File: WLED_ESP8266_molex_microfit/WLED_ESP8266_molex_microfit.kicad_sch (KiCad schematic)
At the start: 62 parts, among them J1 Molex Micro-fit 2x1, J2 Molex Micro-fit 3x1, J3 Molex Micro-fit 2x1, J4 Molex Micro-fit 2x1, J6 Molex Micro-fit 2x1, J7 Molex Micro-fit 3x1, J8 Molex Micro-fit 3x1, Q1 AO3401A, Q2 AO3401A, U1 ESP-12F, U2 TPS54331DDAR, U3 TXS0102DCT, U4 TXS0102DCT, U6 ME6211A33M3G-N

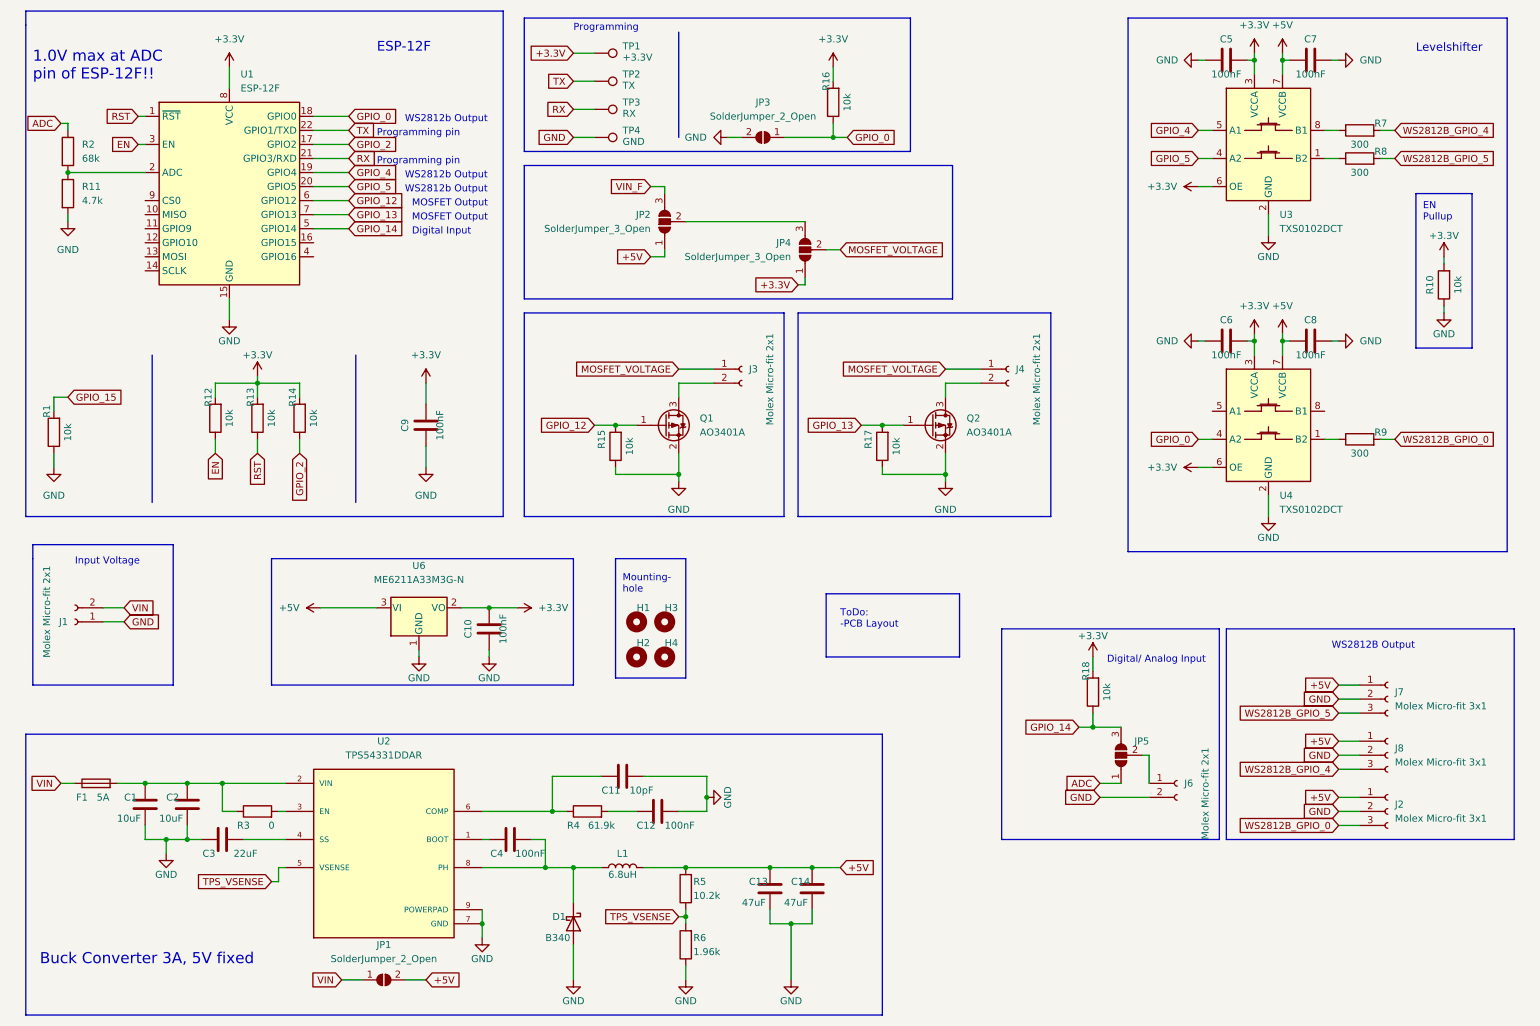
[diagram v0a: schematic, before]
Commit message: USB added
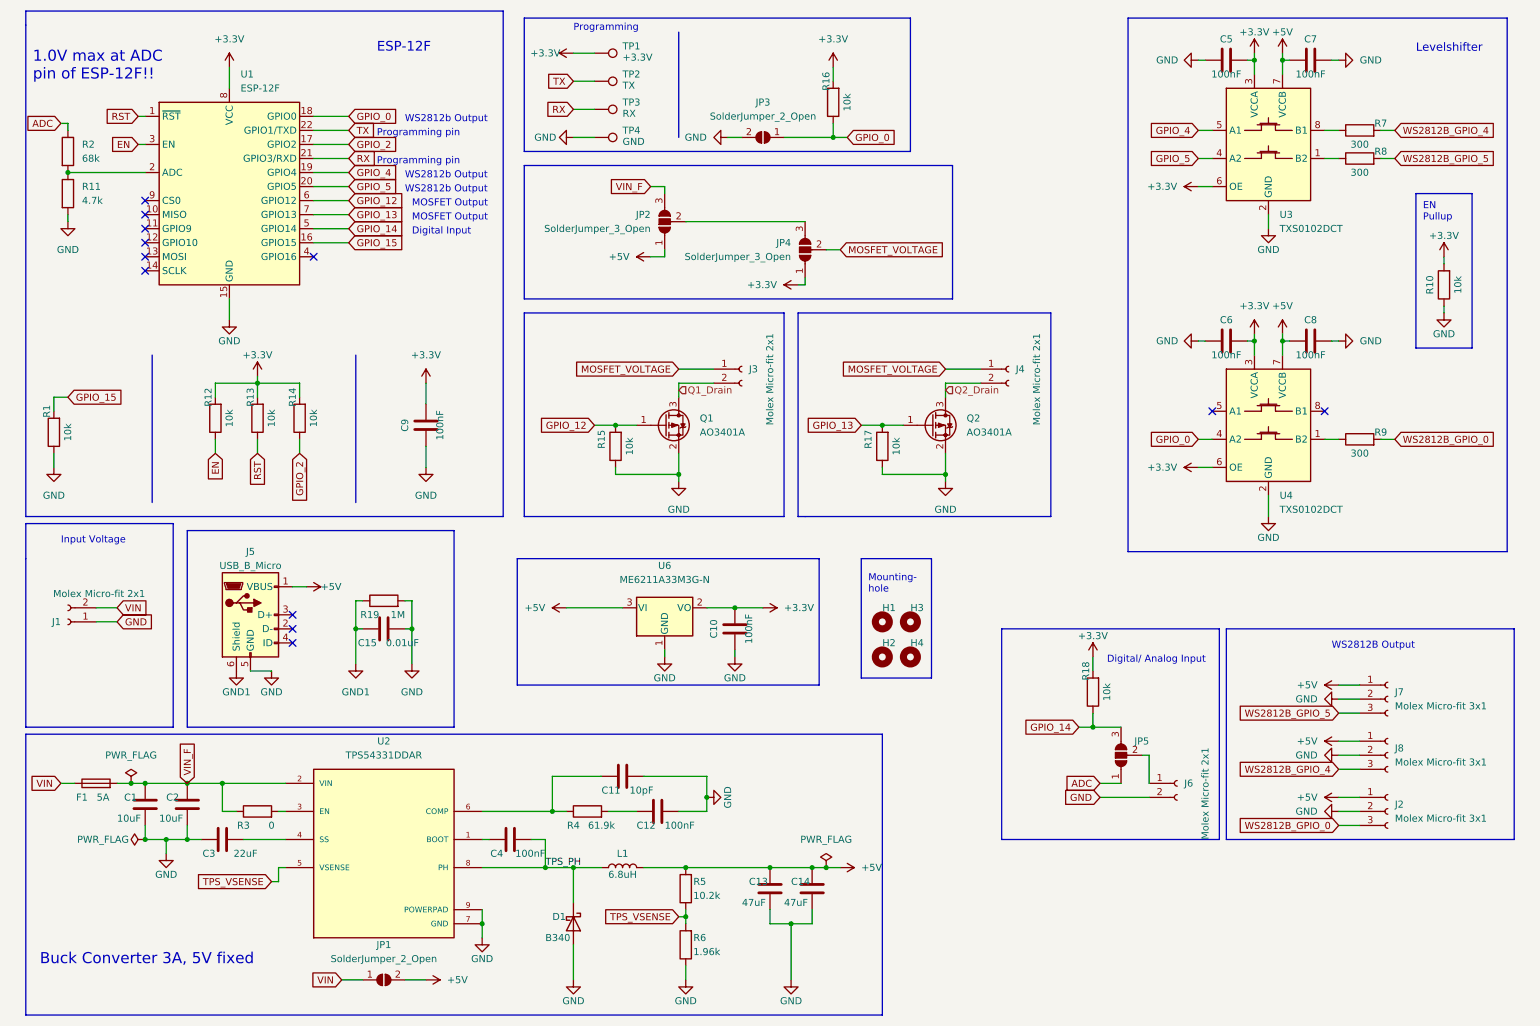
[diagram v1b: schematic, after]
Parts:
- added C15: 0.01uF, Capacitor_SMD:C_0805_2012Metric, symbol Device:C
- added J5: USB_B_Micro, Connector_USB:USB_Micro-B_Molex_47346-0001, symbol Connector:USB_B_Micro
- added R19: 1M, Resistor_SMD:R_0805_2012Metric, symbol Device:R
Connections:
- net +3.3V is gone; now on net +3V3: JP4.1 (A), TP1.1
- net +5V: now also J5.1 (VBUS)
- net GND: now also C15.2, J5.5 (GND), R19.2
- net GPIO_15: now also U1.16 (GPIO15)
- net VIN_F: now also C1.1, C2.1, F1.2, R3.1, U2.2 (VIN)
- net Q1_Drain: now reaches J3.2 (Pin_2), Q1.3 (D)
- net TPS_PH: now reaches C4.2, D1.1 (K), L1.1, U2.8 (PH)
- net Q2_Drain: now reaches J4.2 (Pin_2), Q2.3 (D)
- new net GND1: C15.1, J5.6 (Shield), R19.1
- no-connect marks 0 -> 12
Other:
- note removed: "ToDo: -PCB Layout"
- moved on the sheet: C10, H1, H2, H3, H4, J1, U6

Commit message: Issue 28.01.Yannik_part1
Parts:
- R1, R10, R12, R13, R14, R15, R16, R17: footprint Capacitor_SMD:C_0402_1005Metric_Pad0.74x0.62mm_HandSolder -> Resistor_SMD:R_0402_1005Metric_Pad0.72x0.64mm_HandSolder
- R18, R7, R8, R9: footprint Capacitor_SMD:C_0603_1608Metric_Pad1.08x0.95mm_HandSolder -> Resistor_SMD:R_0603_1608Metric_Pad0.98x0.95mm_HandSolder
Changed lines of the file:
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@@
     (property "Reference" "R12" (id 0) (at 46.99 83.82 90))
     (property "Value" "10k" (id 1) (at 50.8 87.63 90))
-    (property "Footprint" "Capacitor_SMD:C_0402_1005Metric_Pad0.74x0.62mm_HandSolder" (id 2) (at 50.038 87.63 90)
+    (property "Footprint" "Resistor_SMD:R_0402_1005Metric_Pad0.72x0.64mm_HandSolder" (id 2) (at 50.038 87.63 90)
       (effects (font (size 1.27 1.27)) hide)
     )
@@
     (property "Reference" "R8" (id 0) (at 259.08 39.37 90))
     (property "Value" "300" (id 1) (at 255.27 43.18 90))
-    (property "Footprint" "Capacitor_SMD:C_0603_1608Metric_Pad1.08x0.95mm_HandSolder" (id 2) (at 255.27 42.418 90)
+    (property "Footprint" "Resistor_SMD:R_0603_1608Metric_Pad0.98x0.95mm_HandSolder" (id 2) (at 255.27 42.418 90)
       (effects (font (size 1.27 1.27)) hide)
     )
@@
     (property "Reference" "R17" (id 0) (at 166.37 91.44 90))
     (property "Value" "10k" (id 1) (at 171.45 92.71 90))
-    (property "Footprint" "Capacitor_SMD:C_0402_1005Metric_Pad0.74x0.62mm_HandSolder" (id 2) (at 170.688 92.71 90)
+    (property "Footprint" "Resistor_SMD:R_0402_1005Metric_Pad0.72x0.64mm_HandSolder" (id 2) (at 170.688 92.71 90)
       (effects (font (size 1.27 1.27)) hide)
     )
@@
     (property "Reference" "R15" (id 0) (at 118.11 91.44 90))
     (property "Value" "10k" (id 1) (at 123.19 92.71 90))
-    (property "Footprint" "Capacitor_SMD:C_0402_1005Metric_Pad0.74x0.62mm_HandSolder" (id 2) (at 122.428 92.71 90)
+    (property "Footprint" "Resistor_SMD:R_0402_1005Metric_Pad0.72x0.64mm_HandSolder" (id 2) (at 122.428 92.71 90)
       (effects (font (size 1.27 1.27)) hide)
     )
@@
     (property "Reference" "R9" (id 0) (at 259.08 90.17 90))
     (property "Value" "300" (id 1) (at 255.27 93.98 90))
-    (property "Footprint" "Capacitor_SMD:C_0603_1608Metric_Pad1.08x0.95mm_HandSolder" (id 2) (at 255.27 93.218 90)
+    (property "Footprint" "Resistor_SMD:R_0603_1608Metric_Pad0.98x0.95mm_HandSolder" (id 2) (at 255.27 93.218 90)
       (effects (font (size 1.27 1.27)) hide)
     )
@@
     (property "Reference" "R14" (id 0) (at 62.23 83.82 90))
     (property "Value" "10k" (id 1) (at 66.04 87.63 90))
-    (property "Footprint" "Capacitor_SMD:C_0402_1005Metric_Pad0.74x0.62mm_HandSolder" (id 2) (at 65.278 87.63 90)
+    (property "Footprint" "Resistor_SMD:R_0402_1005Metric_Pad0.72x0.64mm_HandSolder" (id 2) (at 65.278 87.63 90)
       (effects (font (size 1.27 1.27)) hide)
     )
@@
     (property "Reference" "R7" (id 0) (at 259.08 34.29 90))
     (property "Value" "300" (id 1) (at 255.27 38.1 90))
-    (property "Footprint" "Capacitor_SMD:C_0603_1608Metric_Pad1.08x0.95mm_HandSolder" (id 2) (at 255.27 37.338 90)
+    (property "Footprint" "Resistor_SMD:R_0603_1608Metric_Pad0.98x0.95mm_HandSolder" (id 2) (at 255.27 37.338 90)
       (effects (font (size 1.27 1.27)) hide)
     )
@@
     (property "Reference" "R1" (id 0) (at 17.78 86.36 90))
     (property "Value" "10k" (id 1) (at 21.59 90.17 90))
-    (property "Footprint" "Capacitor_SMD:C_0402_1005Metric_Pad0.74x0.62mm_HandSolder" (id 2) (at 20.828 90.17 90)
+    (property "Footprint" "Resistor_SMD:R_0402_1005Metric_Pad0.72x0.64mm_HandSolder" (id 2) (at 20.828 90.17 90)
       (effects (font (size 1.27 1.27)) hide)
     )
@@
     (property "Reference" "R16" (id 0) (at 158.75 26.67 90))
     (property "Value" "10k" (id 1) (at 162.56 30.48 90))
-    (property "Footprint" "Capacitor_SMD:C_0402_1005Metric_Pad0.74x0.62mm_HandSolder" (id 2) (at 161.798 30.48 90)
+    (property "Footprint" "Resistor_SMD:R_0402_1005Metric_Pad0.72x0.64mm_HandSolder" (id 2) (at 161.798 30.48 90)
       (effects (font (size 1.27 1.27)) hide)
     )
@@
     (property "Reference" "R10" (id 0) (at 267.97 63.5 90))
     (property "Value" "10k" (id 1) (at 273.05 63.5 90))
-    (property "Footprint" "Capacitor_SMD:C_0402_1005Metric_Pad0.74x0.62mm_HandSolder" (id 2) (at 272.288 63.5 90)
+    (property "Footprint" "Resistor_SMD:R_0402_1005Metric_Pad0.72x0.64mm_HandSolder" (id 2) (at 272.288 63.5 90)
       (effects (font (size 1.27 1.27)) hide)
     )
@@
     (property "Reference" "R18" (id 0) (at 205.74 133.35 90))
     (property "Value" "10k" (id 1) (at 209.55 137.16 90))
-    (property "Footprint" "Capacitor_SMD:C_0603_1608Metric_Pad1.08x0.95mm_HandSolder" (id 2) (at 208.788 137.16 90)
+    (property "Footprint" "Resistor_SMD:R_0603_1608Metric_Pad0.98x0.95mm_HandSolder" (id 2) (at 208.788 137.16 90)
       (effects (font (size 1.27 1.27)) hide)
     )
@@
     (property "Reference" "R13" (id 0) (at 54.61 83.82 90))
     (property "Value" "10k" (id 1) (at 58.42 87.63 90))
-    (property "Footprint" "Capacitor_SMD:C_0402_1005Metric_Pad0.74x0.62mm_HandSolder" (id 2) (at 57.658 87.63 90)
+    (property "Footprint" "Resistor_SMD:R_0402_1005Metric_Pad0.72x0.64mm_HandSolder" (id 2) (at 57.658 87.63 90)
       (effects (font (size 1.27 1.27)) hide)
     )
@@
     )
     (path "/d73f5447-4ae0-4c4a-a809-adb19f1201cd"
-      (reference "R1") (unit 1) (value "10k") (footprint "Capacitor_SMD:C_0402_1005Metric_Pad0.74x0.62mm_HandSolder")
+      (reference "R1") (unit 1) (value "10k") (footprint "Resistor_SMD:R_0402_1005Metric_Pad0.72x0.64mm_HandSolder")
     )
     (path "/9736f88a-f61b-412c-91c8-9d84934592a6"
@@
     )
     (path "/d25a3270-010c-46c6-957f-123f9bf187b7"
-      (reference "R7") (unit 1) (value "300") (footprint "Capacitor_SMD:C_0603_1608Metric_Pad1.08x0.95mm_HandSolder")
+      (reference "R7") (unit 1) (value "300") (footprint "Resistor_SMD:R_0603_1608Metric_Pad0.98x0.95mm_HandSolder")
     )
     (path "/41178f10-9942-424b-8ecb-9661f254316d"
-      (reference "R8") (unit 1) (value "300") (footprint "Capacitor_SMD:C_0603_1608Metric_Pad1.08x0.95mm_HandSolder")
+      (reference "R8") (unit 1) (value "300") (footprint "Resistor_SMD:R_0603_1608Metric_Pad0.98x0.95mm_HandSolder")
     )
     (path "/984f9213-4deb-4eff-b095-cde2ceafdd01"
-      (reference "R9") (unit 1) (value "300") (footprint "Capacitor_SMD:C_0603_1608Metric_Pad1.08x0.95mm_HandSolder")
+      (reference "R9") (unit 1) (value "300") (footprint "Resistor_SMD:R_0603_1608Metric_Pad0.98x0.95mm_HandSolder")
     )
     (path "/e21af3ac-6a90-40ab-8522-34cb00684b27"
-      (reference "R10") (unit 1) (value "10k") (footprint "Capacitor_SMD:C_0402_1005Metric_Pad0.74x0.62mm_HandSolder")
+      (reference "R10") (unit 1) (value "10k") (footprint "Resistor_SMD:R_0402_1005Metric_Pad0.72x0.64mm_HandSolder")
     )
     (path "/5aef3f3d-e3a1-42e7-aab5-b97ecd4f9ebd"
@@
     )
     (path "/0526c0f0-b604-4a5d-b668-a554f7870c57"
-      (reference "R12") (unit 1) (value "10k") (footprint "Capacitor_SMD:C_0402_1005Metric_Pad0.74x0.62mm_HandSolder")
+      (reference "R12") (unit 1) (value "10k") (footprint "Resistor_SMD:R_0402_1005Metric_Pad0.72x0.64mm_HandSolder")
     )
     (path "/f9fe30f9-fa00-46d5-a4e6-77d63a55d4b6"
-      (reference "R13") (unit 1) (value "10k") (footprint "Capacitor_SMD:C_0402_1005Metric_Pad0.74x0.62mm_HandSolder")
+      (reference "R13") (unit 1) (value "10k") (footprint "Resistor_SMD:R_0402_1005Metric_Pad0.72x0.64mm_HandSolder")
     )
     (path "/c462ec9b-ec5e-4e59-b306-0da8d6f70500"
-      (reference "R14") (unit 1) (value "10k") (footprint "Capacitor_SMD:C_0402_1005Metric_Pad0.74x0.62mm_HandSolder")
+      (reference "R14") (unit 1) (value "10k") (footprint "Resistor_SMD:R_0402_1005Metric_Pad0.72x0.64mm_HandSolder")
     )
     (path "/8bdcca36-89f8-4cc2-867e-e40b791a0029"
-      (reference "R15") (unit 1) (value "10k") (footprint "Capacitor_SMD:C_0402_1005Metric_Pad0.74x0.62mm_HandSolder")
+      (reference "R15") (unit 1) (value "10k") (footprint "Resistor_SMD:R_0402_1005Metric_Pad0.72x0.64mm_HandSolder")
     )
     (path "/d7a72f02-1984-4a3c-9afb-0ee7d0f20433"
-      (reference "R16") (unit 1) (value "10k") (footprint "Capacitor_SMD:C_0402_1005Metric_Pad0.74x0.62mm_HandSolder")
+      (reference "R16") (unit 1) (value "10k") (footprint "Resistor_SMD:R_0402_1005Metric_Pad0.72x0.64mm_HandSolder")
     )
     (path "/59799987-08dc-4288-9480-cfc9b65b7e76"
-      (reference "R17") (unit 1) (value "10k") (footprint "Capacitor_SMD:C_0402_1005Metric_Pad0.74x0.62mm_HandSolder")
+      (reference "R17") (unit 1) (value "10k") (footprint "Resistor_SMD:R_0402_1005Metric_Pad0.72x0.64mm_HandSolder")
     )
     (path "/f4a3769e-c888-4155-84d6-34953043327d"
-      (reference "R18") (unit 1) (value "10k") (footprint "Capacitor_SMD:C_0603_1608Metric_Pad1.08x0.95mm_HandSolder")
+      (reference "R18") (unit 1) (value "10k") (footprint "Resistor_SMD:R_0603_1608Metric_Pad0.98x0.95mm_HandSolder")
     )
     (path "/be1aa7ed-93c7-4da1-a65d-02d064f41f29"
